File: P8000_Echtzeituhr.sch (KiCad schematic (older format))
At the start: 14 parts, among them X1 Socket-DIN41612-96Pin-3row

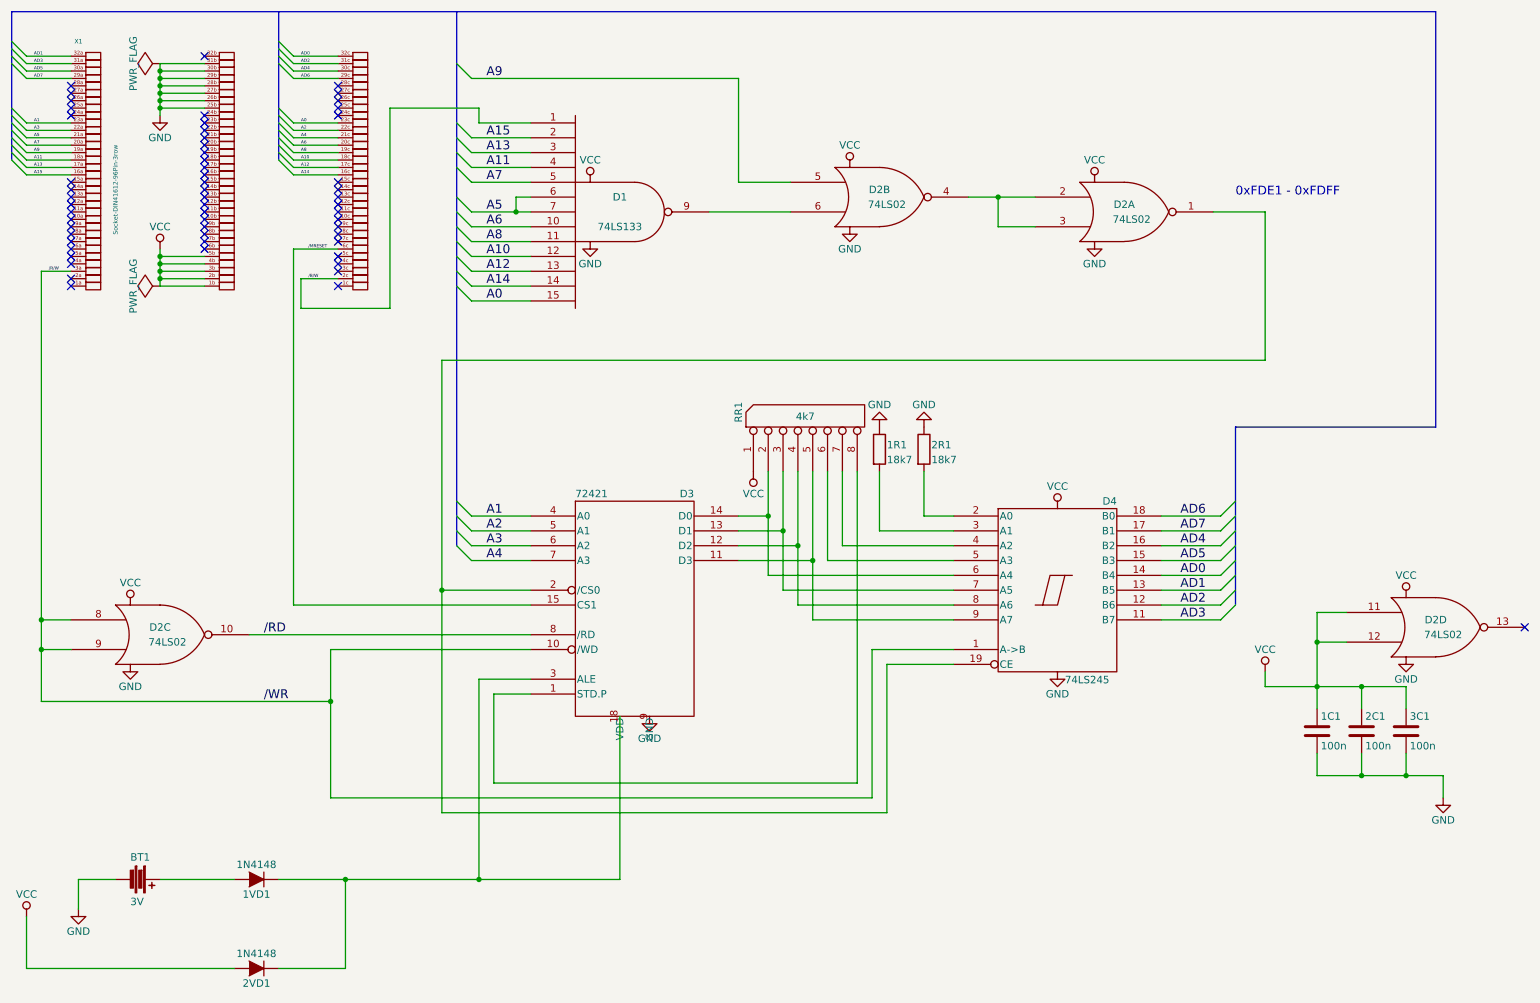
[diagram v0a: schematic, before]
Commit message: fix errors from version 1.1
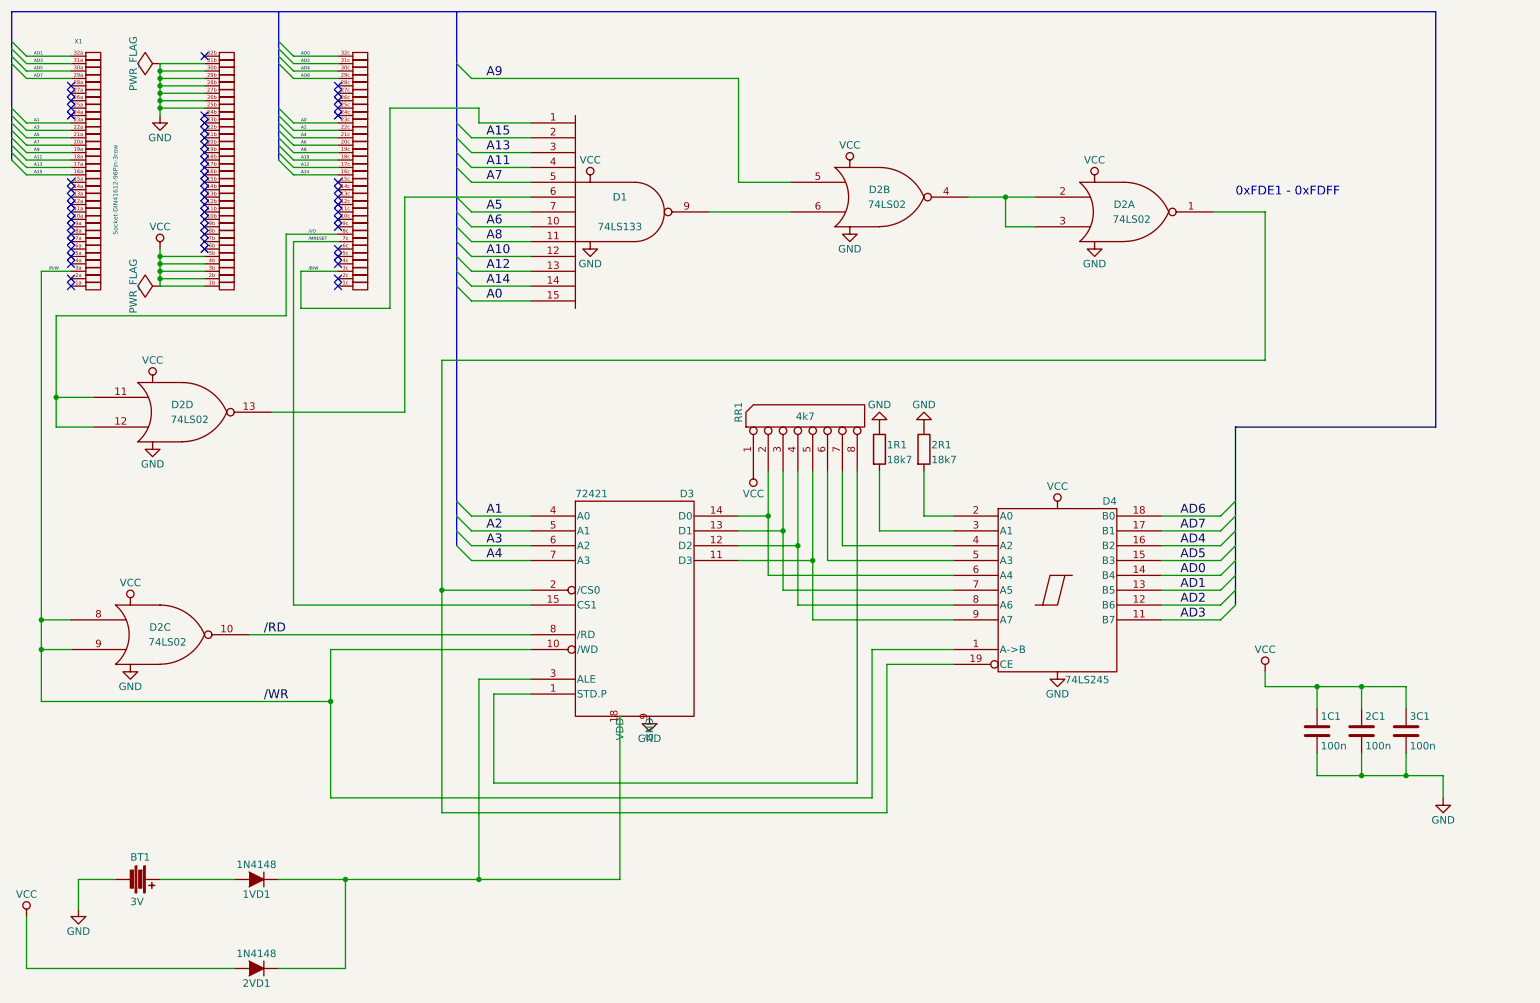
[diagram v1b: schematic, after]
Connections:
- net /B/W: now also X1.3c; no longer X1.2c
- net /MRESET: now also X1.7c; no longer X1.6c
- net A5: no longer D1.6
- net VCC: no longer D2.11, D2.12
- net at D2.13: now also D1.6
- net /I/O: now reaches X1.8c
- net /I/O: now also D2.11, D2.12
- no-connect marks 58 -> 56
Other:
- moved on the sheet: D2D
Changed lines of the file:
@@
 Sheet 1 1
 Title "P8000 Echtzeituhr"
-Date "2016-07-03"
-Rev "1.6"
+Date "2016-07-11"
+Rev "1.7"
 Comp "Oliver Lehmann"
 Comment1 ""
@@
 Entry Wire Line
 	3650 2400 3750 2500
-Text Label 2650 2550 0    21   ~ 0
+Text Label 2650 2500 0    21   ~ 0
 /B/W
 Text Label 3850 1200 0    60   ~ 0
@@
 Text Label 900  2500 0    21   ~ 0
 /R/W
-Text Label 2650 2350 0    21   ~ 0
+Text Label 2650 2300 0    21   ~ 0
 /MRESET
 Text Label 2350 5400 0    60   ~ 0
@@
 L 74LS02 D2
 U 4 1 577186A0
-P 10250 4900
-F 0 "D2" H 10250 4950 50  0000 C CNN
-F 1 "74LS02" H 10300 4850 50  0000 C CNN
-F 2 "Housings_DIP:DIP-14_W7.62mm" H 10250 4900 50  0001 C CNN
-F 3 "" H 10250 4900 50  0000 C CNN
-	4    10250 4900
-	1    0    0    -1
-$EndComp
-NoConn ~ 10850 4900
+P 1800 3450
+F 0 "D2" H 1800 3500 50  0000 C CNN
+F 1 "74LS02" H 1850 3400 50  0000 C CNN
+F 2 "Housings_DIP:DIP-14_W7.62mm" H 1800 3450 50  0001 C CNN
+F 3 "" H 1800 3450 50  0000 C CNN
+	4    1800 3450
+	1    0    0    -1
+$EndComp
 $Comp
 L VCC #PWR08
@@
 NoConn ~ 2850 2200
 NoConn ~ 2850 2150
-NoConn ~ 2850 2250
-NoConn ~ 2850 2300
+NoConn ~ 2850 2350
 NoConn ~ 2850 2400
 NoConn ~ 2850 2450
-NoConn ~ 2850 2500
+NoConn ~ 2850 2550
 NoConn ~ 2850 2600
 $Comp
@@
 L VCC #PWR015
 U 1 1 5771BDAC
-P 10050 4700
-F 0 "#PWR015" H 10050 4550 50  0001 C CNN
-F 1 "VCC" H 10050 4850 50  0000 C CNN
-F 2 "" H 10050 4700 50  0000 C CNN
-F 3 "" H 10050 4700 50  0000 C CNN
-	1    10050 4700
+P 1600 3250
+F 0 "#PWR015" H 1600 3100 50  0001 C CNN
+F 1 "VCC" H 1600 3400 50  0000 C CNN
+F 2 "" H 1600 3250 50  0000 C CNN
+F 3 "" H 1600 3250 50  0000 C CNN
+	1    1600 3250
 	1    0    0    -1
 $EndComp
@@
 L GND #PWR017
 U 1 1 5771C284
-P 10050 5100
-F 0 "#PWR017" H 10050 4850 50  0001 C CNN
-F 1 "GND" H 10050 4950 50  0000 C CNN
-F 2 "" H 10050 5100 50  0000 C CNN
-F 3 "" H 10050 5100 50  0000 C CNN
-	1    10050 5100
+P 1600 3650
+F 0 "#PWR017" H 1600 3400 50  0001 C CNN
+F 1 "GND" H 1600 3500 50  0000 C CNN
+F 2 "" H 1600 3650 50  0000 C CNN
+F 3 "" H 1600 3650 50  0000 C CNN
+	1    1600 3650
 	1    0    0    -1
 $EndComp
@@
 	3650 750  3650 4350
 Wire Wire Line
-	3200 2750 2600 2750
-Wire Wire Line
-	2600 2750 2600 2550
-Wire Wire Line
-	2600 2550 2850 2550
+	2600 2750 3200 2750
+Wire Wire Line
+	2600 2500 2600 2750
 Wire Wire Line
 	3750 1200 5550 1200
@@
 Wire Wire Line
 	7100 2000 7550 2000
-Wire Wire Line
-	7550 2200 7300 2200
-Wire Wire Line
-	7300 2200 7300 2000
-Connection ~ 7300 2000
 Wire Wire Line
 	4150 4150 3750 4150
@@
 	2800 6050 6450 6050
 Wire Wire Line
-	2800 6050 2800 5050
+	2800 5050 2800 6050
 Wire Wire Line
 	2800 5050 4150 5050
@@
 Connection ~ 850  4850
 Wire Wire Line
-	4150 4750 2550 4750
-Wire Wire Line
-	2550 4750 2550 2350
-Wire Wire Line
-	2550 2350 2850 2350
+	2550 4750 4150 4750
+Wire Wire Line
+	2550 2300 2550 4750
 Wire Bus Line
 	10250 750  10250 3550
@@
 Connection ~ 9750 5300
 Wire Wire Line
-	9450 4800 9450 5450
+	9450 5300 9450 5450
 Connection ~ 9450 5300
 Wire Wire Line
@@
 	10050 5750 10050 5900
 Connection ~ 10050 5900
-Wire Wire Line
-	9650 4800 9450 4800
-Wire Wire Line
-	9650 5000 9450 5000
-Connection ~ 9450 5000
 Wire Wire Line
 	1650 2600 1950 2600
@@
 	5350 2100 5900 2100
 Wire Wire Line
-	3200 1400 3200 2750
+	3200 2750 3200 1400
 Wire Wire Line
 	4150 1600 3750 1600
@@
 Text Label 3850 2100 0    60   ~ 0
 A5
-Wire Wire Line
-	4150 2000 4050 2000
-Wire Wire Line
-	4050 2000 4050 2100
-Connection ~ 4050 2100
 Wire Wire Line
 	5950 3850 5950 4750
@@
 	1    0    0    -1
 $EndComp
+Wire Wire Line
+	2850 2500 2600 2500
+Wire Wire Line
+	2850 2300 2550 2300
+Wire Wire Line
+	7550 2200 7350 2200
+Wire Wire Line
+	2500 2800 2500 2250
+Wire Wire Line
+	2500 2250 2850 2250
+Text Label 2650 2250 0    21   ~ 0
+/I/O
+Wire Wire Line
+	7350 2200 7350 2000
+Connection ~ 7350 2000
+Wire Wire Line
+	950  3550 1200 3550
+Wire Wire Line
+	950  2800 950  3550
+Wire Wire Line
+	950  2800 2500 2800
+Wire Wire Line
+	1200 3350 950  3350
+Connection ~ 950  3350
+Wire Wire Line
+	3300 2000 4150 2000
+Wire Wire Line
+	3300 2000 3300 3450
+Wire Wire Line
+	3300 3450 2400 3450
 $EndSCHEMATC
